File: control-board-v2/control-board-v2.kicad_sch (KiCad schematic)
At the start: 110 parts, among them J1 Conn_01x03, J12 Conn_01x01_Pin, J13 Conn_01x01_Pin, J14 Conn_01x02, J15 Conn_01x01_Pin, J16 Conn_01x02, J17 Conn_01x02, J18 Conn_01x02, J19 Conn_01x01_Pin, J2 GPS_ANT, J20 Conn_01x01_Pin, J21 Conn_01x01_Pin, J22 Conn_01x01_Pin, J23 Conn_01x01_Pin, J24 Conn_01x01_Pin, J25 Conn_01x01_Pin, J26 Conn_01x01_Pin, J27 Conn_01x01_Pin, J28 Conn_01x01_Pin, J29 Conn_01x01_Pin, J3 Conn_01x01_Pin, J6 USB_C_Receptacle_USB2.0_16P, J7 Conn_01x01_Pin, U2 NEO-XM, U3 TCAN1462VDRQ1, U5 STM32H563RGTx, U6 AMS1117-3.3, U7 TCAN1462VDRQ1, U8 AP63200WU, Y1 25M

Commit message: feat: ctrl board-v2: add sd card, iso can
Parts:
- removed C28: 1u, Capacitor_SMD:C_0805_2012Metric, symbol Device:C_Small
- removed D11: DESD2CAN2SOQ, Package_TO_SOT_SMD:TSOT-23, symbol Device:D_TVS_Dual_AAC
- removed JP2: Jumper_2_Open, TestPoint:TestPoint_2Pads_Pitch2.54mm_Drill0.8mm, symbol Jumper:Jumper_2_Open
- removed U7: TCAN1462VDRQ1, Package_SO:SOIC-8_3.9x4.9mm_P1.27mm, symbol Interface_CAN_LIN:SN65HVD256D
- added C12: 1u, Capacitor_SMD:C_0805_2012Metric, symbol Device:C_Small
- added C13, C14: 100n, Capacitor_SMD:C_0603_1608Metric, symbol Device:C_Small
- added C38: 10u, Capacitor_SMD:C_0805_2012Metric, symbol Device:C_Small
- added D5: DESD2CAN2SOQ, Package_TO_SOT_SMD:TSOT-23, symbol Device:D_TVS_Dual_AAC
- added D7: LED, LED_SMD:LED_0805_2012Metric, symbol Device:LED
- added J4: Micro_SD_Card_Det1, microSD:microSD_HC_Molex_47219-2001, symbol Connector:Micro_SD_Card_Det1
- added J5: Conn_01x01_Pin, Connector_PinHeader_2.54mm:PinHeader_1x01_P2.54mm_Vertical, symbol Connector:Conn_01x01_Pin
- added JP3: Jumper_2_Open, TestPoint:TestPoint_2Pads_Pitch2.54mm_Drill0.8mm, symbol Jumper:Jumper_2_Open
- added R17, R18: 60R, Resistor_SMD:R_0603_1608Metric, symbol Device:R_Small
- added R26, R27, R28, R29: 10k, Resistor_SMD:R_0603_1608Metric, symbol Device:R_Small
- added TP5: TP_iso5V, TestPoint:TestPoint_THTPad_D1.5mm_Drill0.7mm, symbol Connector:TestPoint
- added U1: ISO1042-Q1, Package_SO:SOIC-8_3.9x4.9mm_P1.27mm, symbol Interface_CAN_LIN:ISO1044BD
- added U4: SCT01F24S05, Converter_DCDC:Converter_DCDC_TRACO_TME_24xxS_Single_THT, symbol Converter_DCDC:TME-2405S
- C25: value 100n -> 1u; footprint Capacitor_SMD:C_0603_1608Metric -> Capacitor_SMD:C_0805_2012Metric
- L1: footprint Inductor_SMD:L_Coilcraft_XAL6060-XXX -> Inductor_SMD:L_0805_2012Metric
- R5, R6: value 60R -> 10k
- TP3: value TP_15V -> TP_24V
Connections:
- net +3V3: now also C26.1, R5.1, R6.1, C14.1, J4.4 (VDD), R26.1, R27.1, R28.1, U1.1 (VCC1)
- net +5V: no longer C26.1
- net CAN2_N: now also D5.1 (A1), R18.2, U1.5 (CANL); no longer R6.2
- net CAN2_P: now also D5.2 (A2), JP3.1 (A), U1.6 (CANH)
- net CAN2_RX: now also U5.33 (PB12), U1.3 (RXD); no longer U5.57 (PB5)
- net CAN2_TX: now also U5.34 (PB13), U1.2 (TXD); no longer U5.58 (PB6)
- net GND: now also C14.2, J4.10 (SHIELD), J4.6 (VSS), U1.4 (GND1), U4.1 (-Vin); no longer H3.1
- net SPI3_SCK: now reaches U5.51 (PC10)
- net SPI3_SCK: now also J4.5 (CLK), R26.2
- net SPI3_MISO: now reaches U5.52 (PC11)
- net SPI3_MISO: now also J4.7 (DAT0), R27.2
- net SPI3_MOSI: now reaches U5.53 (PC12)
- net SPI3_MOSI: now also R6.2, J4.3 (CMD)
- net SD_CS: now reaches U5.54 (PD2)
- net SD_CS: now also R5.2, J4.2 (DAT3/CD)
- net +15V renamed +24V
- net +24V: now also U4.2 (+Vin)
- new net: D7.2 (A), R29.2
- new net: JP3.2 (B), R17.1
- new net: C12.1, R17.2, R18.1
- new net: J4.9 (DET), R28.2
- new net +ISO5V: C13.1, C38.1, R29.1, TP5.1, U1.8 (VCC2), U4.4 (+Vout)
- new net Earth: C12.2, C13.2, C38.2, D5.3 (common), D7.1 (K), J5.1 (Pin_1), U1.7 (GND2), U4.3 (-Vout)
- no-connect marks 38 -> 36
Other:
- note added: "Micro SD Card"
- note removed: "Fault signal"
- moved on the sheet: C1, C10, C11, C16, C2, C21, C24, C3, C33, C34, C35, C36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

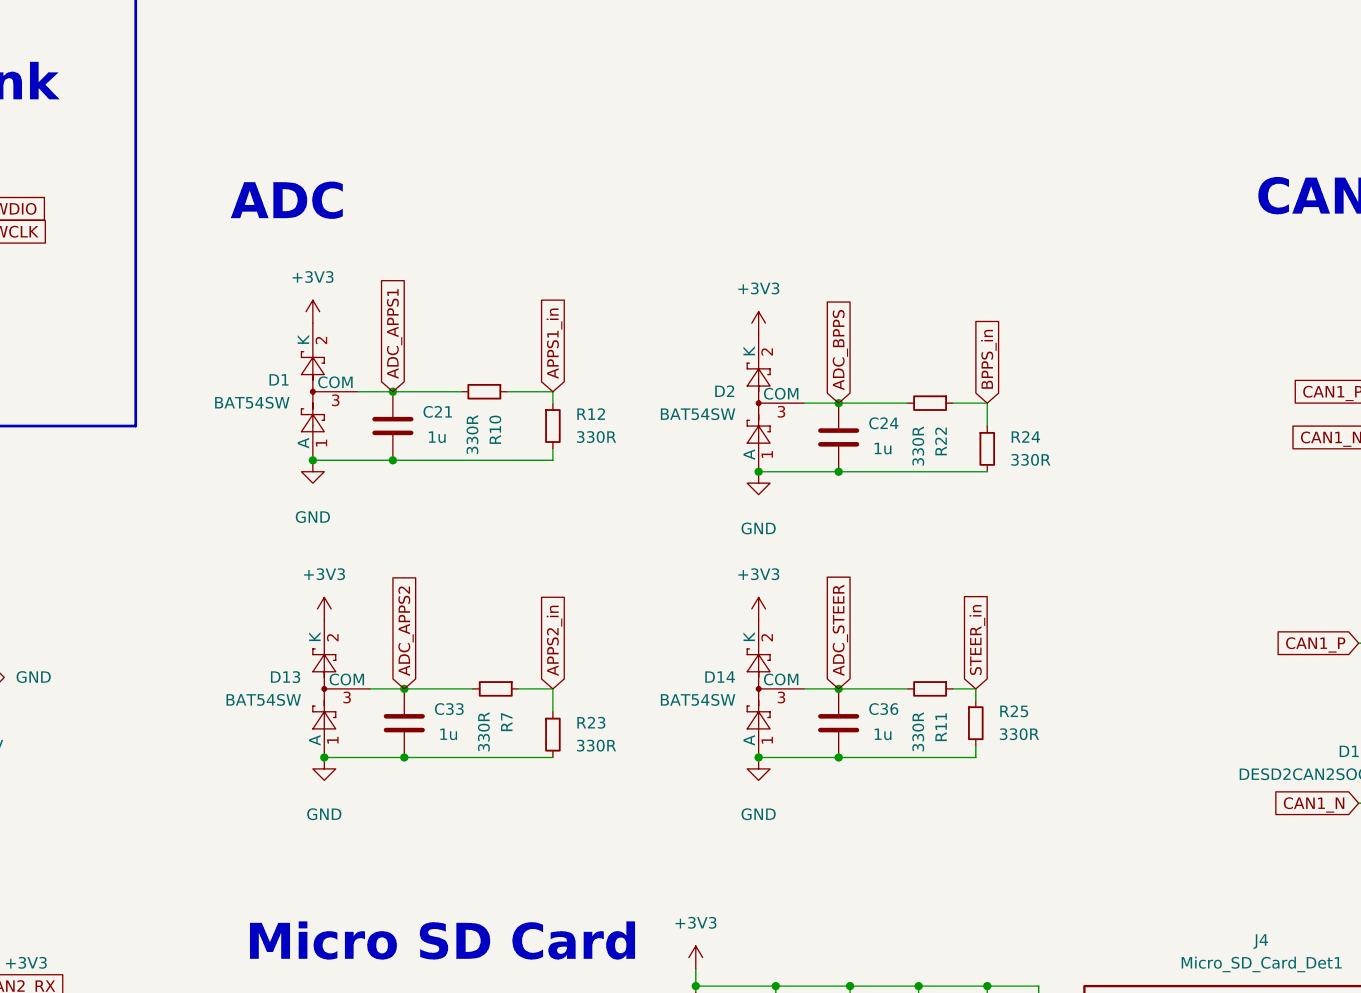
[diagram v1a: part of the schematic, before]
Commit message: fix: schottky diode
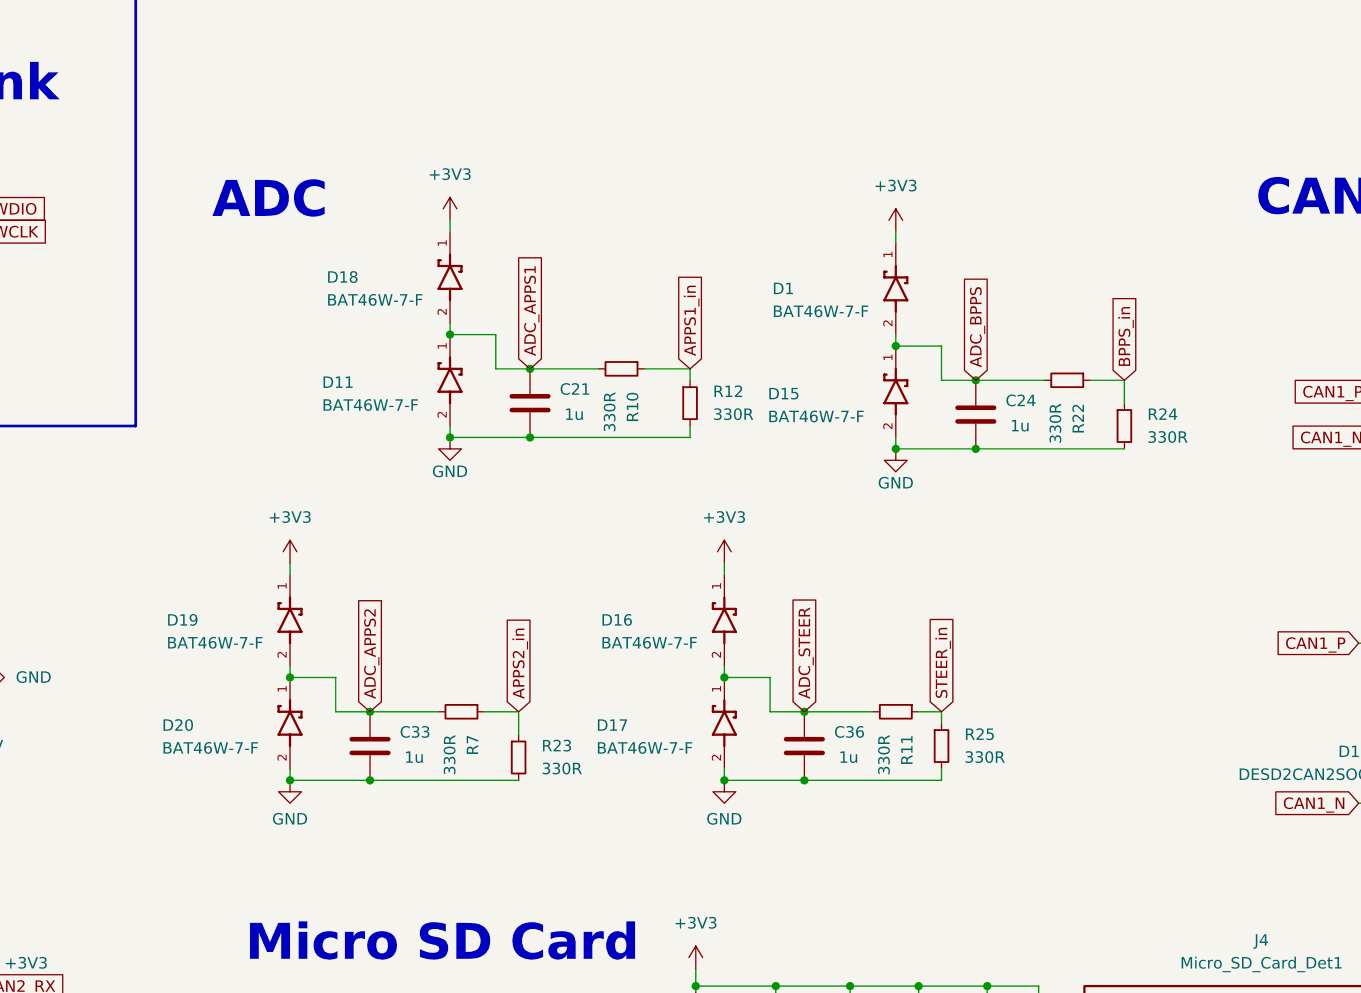
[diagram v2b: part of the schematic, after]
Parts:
- removed D1, D13, D14, D2: BAT54SW, Package_TO_SOT_SMD:SOT-323_SC-70, symbol Diode:BAT54SW
- added D1, D11, D15, D16, D17, D18, D19, D20: BAT46W-7-F, BAT46W-7-F:SOD3715X145N, symbol BAT46W-7-F:BAT46W-7-F
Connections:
- net +3V3: now also D1.1, D16.1, D18.1, D19.1
- net ADC_APPS1: now also D11.1, D18.2
- net ADC_APPS2: now also D19.2, D20.1
- net ADC_BPPS: now also D1.2, D15.1
- net ADC_STEER: now also D16.2, D17.1
- net GND: now also D11.2, D15.2, D17.2, D20.2
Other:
- moved on the sheet: C21, C24, C33, C36, R10, R11, R12, R22, R23, R24, R25, R7
